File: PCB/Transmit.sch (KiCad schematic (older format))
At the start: 27 parts

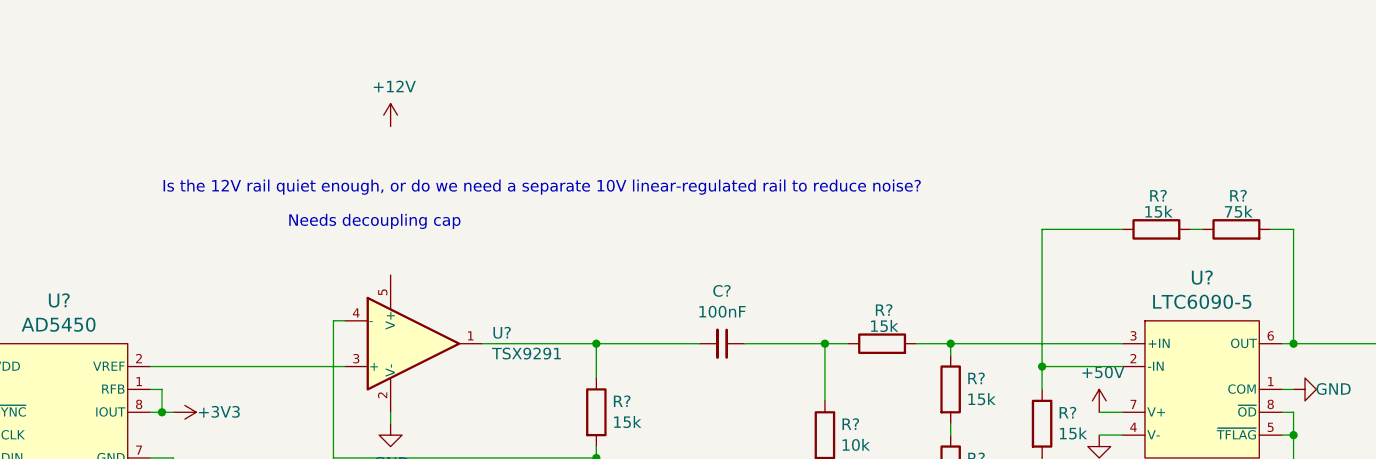
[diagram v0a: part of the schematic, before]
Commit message: Changed transmit-enable to connect to FPGA instead of microcontroller, added 10V linear regulator
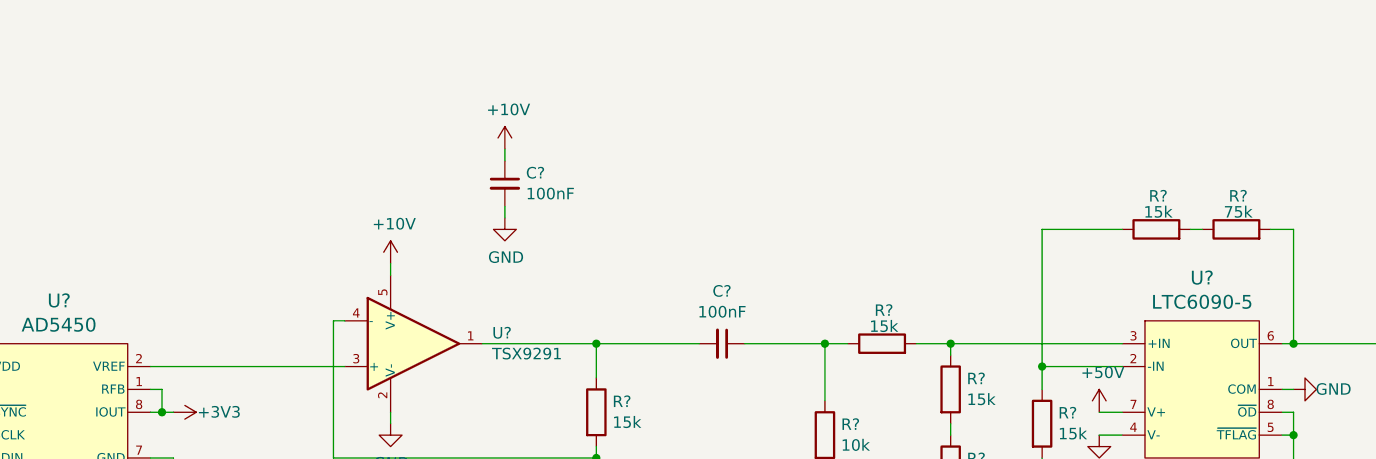
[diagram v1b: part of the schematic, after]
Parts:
- added C?: 100nF, Capacitors_SMD:C_0603_HandSoldering, symbol Device:C_Small
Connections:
- net GND: now also C?.2
- net +10V: now reaches U?.5 (V+)
- net +10V: now also C?.1
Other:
- note removed: "Is the 12V rail quiet enough, or do we need a separate 10V linear-regulated rail to reduce noise?"
- note removed: "Needs decoupling cap"
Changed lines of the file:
@@
 $EndComp
-$Comp
-L power:+12V #PWR?
-U 1 1 5DED5B08
-P 3700 2650
-F 0 "#PWR?" H 3700 2500 50  0001 C CNN
-F 1 "+12V" H 3715 2823 50  0000 C CNN
-F 2 "" H 3700 2650 50  0001 C CNN
-F 3 "" H 3700 2650 50  0001 C CNN
-	1    3700 2650
-	1    0    0    -1
-$EndComp
-Text Notes 2700 2950 0    50   ~ 0
-Is the 12V rail quiet enough, or do we need a separate 10V linear-regulated rail to reduce noise?
 $Comp
 L Device:R R?
@@
 Wire Wire Line
 	8650 5800 8650 5850
-Text Notes 3250 3100 0    50   ~ 0
-Needs decoupling cap
 $Comp
 L power:GND #PWR?
@@
 Wire Wire Line
 	800  3050 800  3100
+$Comp
+L power:+10V #PWR?
+U 1 1 5E0A0743
+P 3700 3250
+F 0 "#PWR?" H 3700 3100 50  0001 C CNN
+F 1 "+10V" H 3715 3423 50  0000 C CNN
+F 2 "" H 3700 3250 50  0001 C CNN
+F 3 "" H 3700 3250 50  0001 C CNN
+	1    3700 3250
+	1    0    0    -1
+$EndComp
+$Comp
+L Device:C_Small C?
+U 1 1 5E1245EE
+P 4200 2900
+F 0 "C?" H 4292 2946 50  0000 L CNN
+F 1 "100nF" H 4292 2855 50  0000 L CNN
+F 2 "Capacitors_SMD:C_0603_HandSoldering" H 4200 2900 50  0001 C CNN
+F 3 "https://www.digikey.ca/product-detail/en/samsung-electro-mechanics/CL10B104KB8NNNC/1276-1000-1-ND/3889086" H 4200 2900 50  0001 C CNN
+	1    4200 2900
+	1    0    0    -1
+$EndComp
+$Comp
+L power:+10V #PWR?
+U 1 1 5E124B96
+P 4200 2750
+F 0 "#PWR?" H 4200 2600 50  0001 C CNN
+F 1 "+10V" H 4215 2923 50  0000 C CNN
+F 2 "" H 4200 2750 50  0001 C CNN
+F 3 "" H 4200 2750 50  0001 C CNN
+	1    4200 2750
+	1    0    0    -1
+$EndComp
+Wire Wire Line
+	4200 2750 4200 2800
+$Comp
+L power:GND #PWR?
+U 1 1 5E1277BF
+P 4200 3050
+F 0 "#PWR?" H 4200 2800 50  0001 C CNN
+F 1 "GND" H 4205 2877 50  0000 C CNN
+F 2 "" H 4200 3050 50  0001 C CNN
+F 3 "" H 4200 3050 50  0001 C CNN
+	1    4200 3050
+	1    0    0    -1
+$EndComp
+Wire Wire Line
+	4200 3050 4200 3000
+Wire Wire Line
+	3700 3250 3700 3300
 $EndSCHEMATC

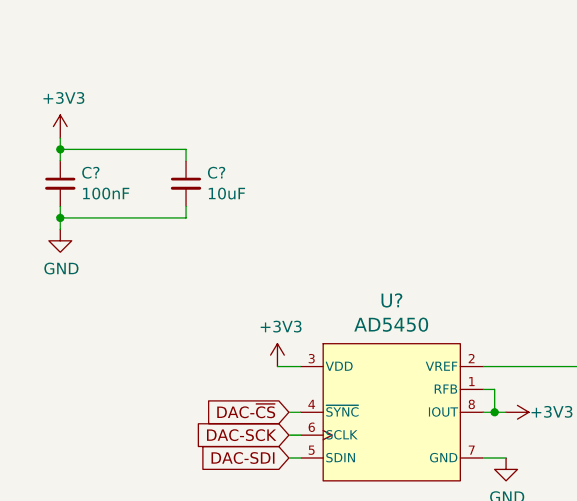
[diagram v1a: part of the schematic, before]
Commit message: Switch 3.3V analog circuitry to low noise supply, fix pin classifications on some parts, swap 9V connector for 10V
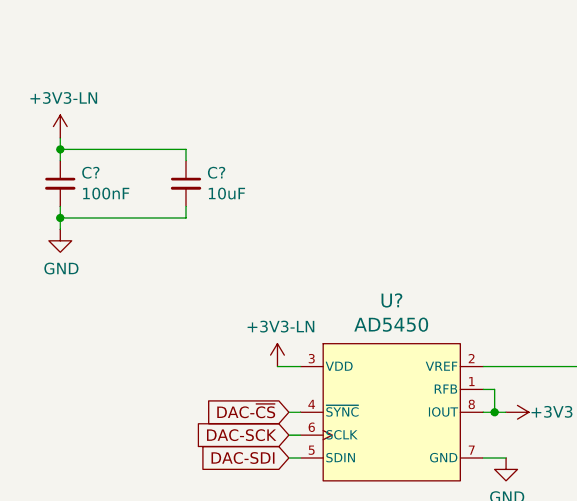
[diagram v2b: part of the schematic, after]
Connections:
- net +3V3: no longer C?.1, C?.1, U?.3 (VDD)
- new net +3V3-LN: C?.1, C?.1, U?.3 (VDD)
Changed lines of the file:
@@
-$EndComp
-$Comp
-L power:+3V3 #PWR?
-U 1 1 5DE63453
-P 1750 3700
-F 0 "#PWR?" H 1750 3550 50  0001 C CNN
-F 1 "+3V3" H 1765 3873 50  0000 C CNN
-F 2 "" H 1750 3700 50  0001 C CNN
-F 3 "" H 1750 3700 50  0001 C CNN
-	1    1750 3700
-	1    0    0    -1
 $EndComp
 $Comp
@@
 $EndComp
 $Comp
-L power:+3V3 #PWR?
-U 1 1 5E3B8767
-P 800 2700
-F 0 "#PWR?" H 800 2550 50  0001 C CNN
-F 1 "+3V3" H 815 2873 50  0000 C CNN
-F 2 "" H 800 2700 50  0001 C CNN
-F 3 "" H 800 2700 50  0001 C CNN
-	1    800  2700
-	1    0    0    -1
-$EndComp
-$Comp
 L Device:C_Small C?
 U 1 1 5E3BD08F
@@
 Wire Wire Line
 	3700 3250 3700 3300
+$Comp
+L Parts:+3V3-LN #PWR?
+U 1 1 5E29A668
+P 1750 3700
+F 0 "#PWR?" H 1750 3550 50  0001 C CNN
+F 1 "+3V3-LN" H 1765 3873 50  0000 C CNN
+F 2 "" H 1750 3700 50  0001 C CNN
+F 3 "" H 1750 3700 50  0001 C CNN
+	1    1750 3700
+	1    0    0    -1
+$EndComp
+$Comp
+L Parts:+3V3-LN #PWR?
+U 1 1 5E29D33A
+P 800 2700
+F 0 "#PWR?" H 800 2550 50  0001 C CNN
+F 1 "+3V3-LN" H 815 2873 50  0000 C CNN
+F 2 "" H 800 2700 50  0001 C CNN
+F 3 "" H 800 2700 50  0001 C CNN
+	1    800  2700
+	1    0    0    -1
+$EndComp
 $EndSCHEMATC

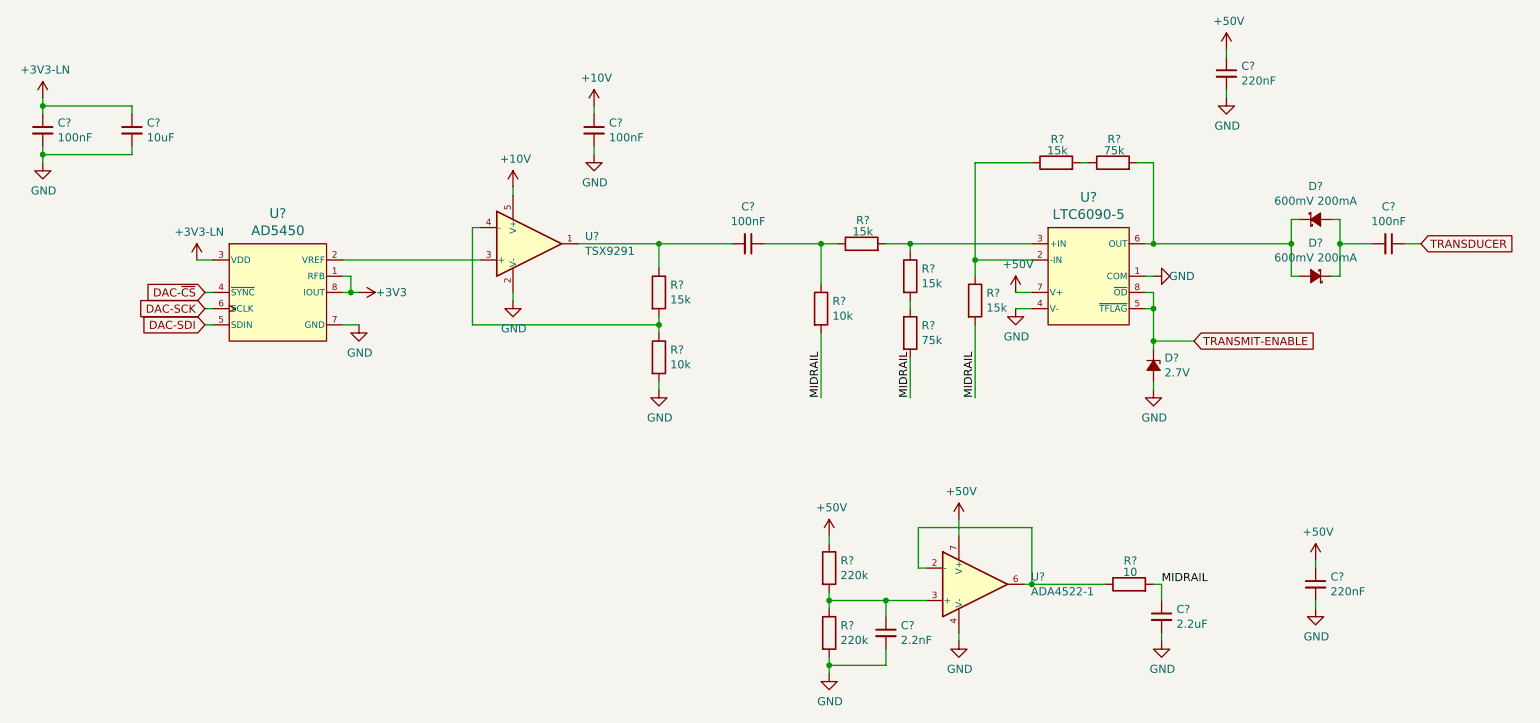
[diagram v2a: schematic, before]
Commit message: Annotate schematic, simplify transmit circuit, shuffle receive opamp stages, reorder buttons so they match net names, reorder connectors to simplify routing, begin arranging parts on PCB
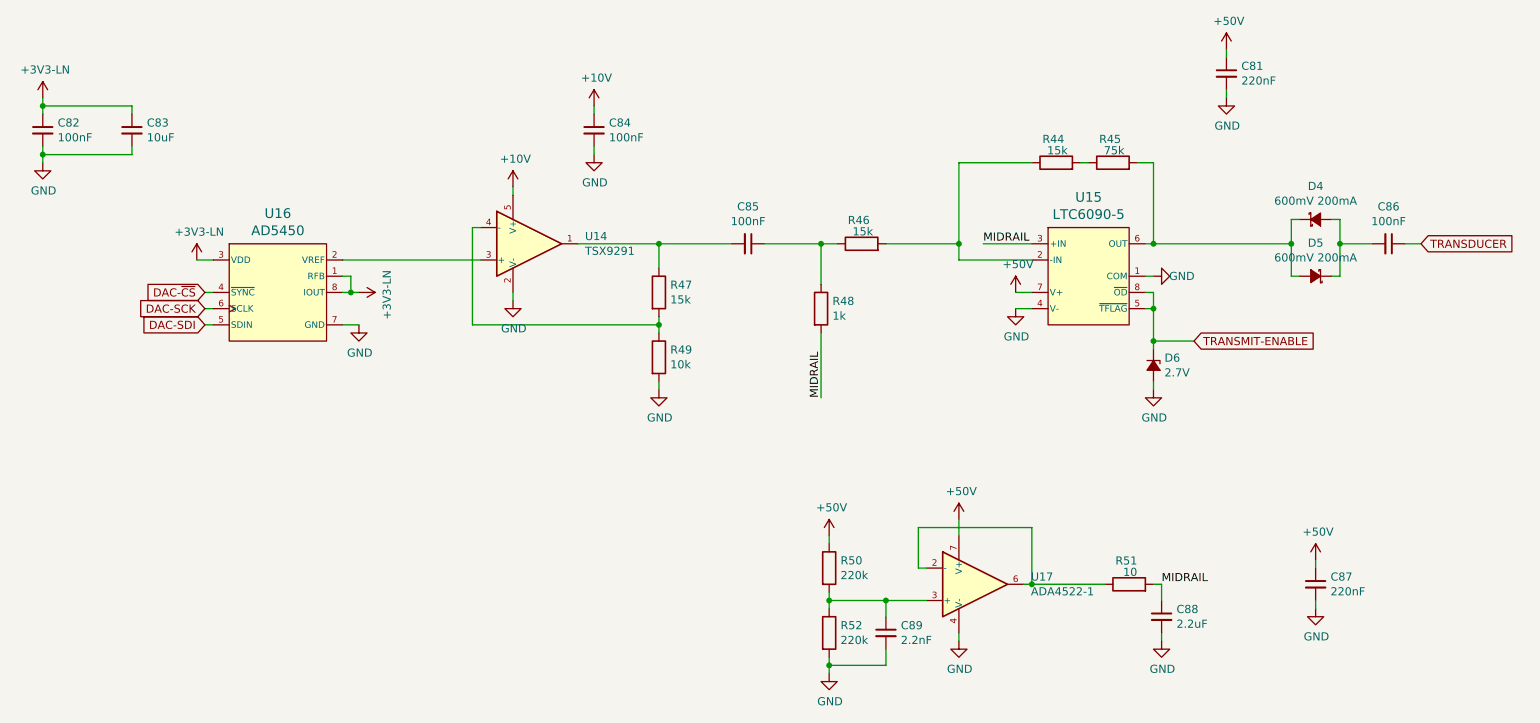
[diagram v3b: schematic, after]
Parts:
- removed R? (x2): 15k, Resistors_SMD:R_0603_HandSoldering, symbol Device:R
- removed R?: 75k, Resistors_SMD:R_0603_HandSoldering, symbol Device:R
- R48: renamed from R?; value 10k -> 1k
- gave numbers to parts that had none: 24
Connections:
- net +3V3 is gone; now on net +3V3-LN: U16.1 (RFB), U16.8 (IOUT)
- net MIDRAIL: now also U15.3 (+IN)
- net at R46.2: now also R44.1, U15.2 (-IN); no longer U15.3 (+IN)

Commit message: Begin layout around FPGA and microcontroller, rearrange some connections to FPGA and microcontroller, change groupings of optional debug pins
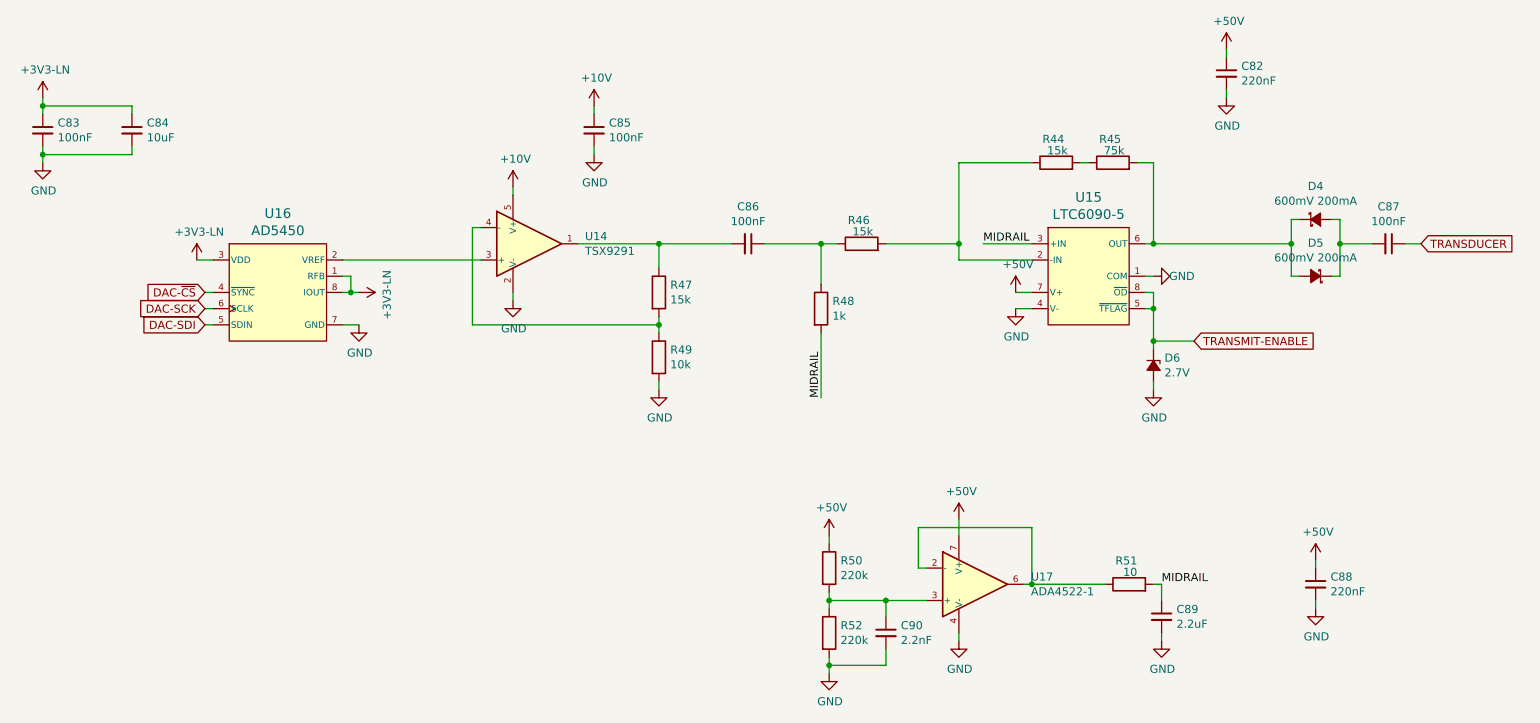
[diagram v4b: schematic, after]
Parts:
- renumbered C81 to C82, C82 to C83, C83 to C84, C84 to C85, C85 to C86, C86 to C87, C87 to C88, C88 to C89, C89 to C90
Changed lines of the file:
@@
 	2650 3700 3500 3700
 $Comp
-L Device:C_Small C85
+L Device:C_Small C86
 U 1 1 5DF03C94
 P 5150 3600
-F 0 "C85" V 4921 3600 50  0000 C CNN
+F 0 "C86" V 4921 3600 50  0000 C CNN
 F 1 "100nF" V 5012 3600 50  0000 C CNN
 F 2 "Capacitors_SMD:C_1206_HandSoldering" H 5150 3600 50  0001 C CNN
@@
 	6450 3100 6900 3100
 $Comp
-L Device:C_Small C86
+L Device:C_Small C87
 U 1 1 5DEF2296
 P 9100 3600
-F 0 "C86" V 8871 3600 50  0000 C CNN
+F 0 "C87" V 8871 3600 50  0000 C CNN
 F 1 "100nF" V 8962 3600 50  0000 C CNN
 F 2 "Capacitors_SMD:C_1206_HandSoldering" H 9100 3600 50  0001 C CNN
@@
 $EndComp
 $Comp
-L Device:C_Small C88
+L Device:C_Small C89
 U 1 1 5DF222FC
 P 7700 5900
-F 0 "C88" H 7792 5946 50  0000 L CNN
+F 0 "C89" H 7792 5946 50  0000 L CNN
 F 1 "2.2uF" H 7792 5855 50  0000 L CNN
 F 2 "Capacitors_SMD:C_1210_HandSoldering" H 7700 5900 50  0001 C CNN
@@
 	7700 5700 7700 5800
 $Comp
-L Device:C_Small C81
+L Device:C_Small C82
 U 1 1 5DF2730B
 P 8100 2550
-F 0 "C81" H 8192 2596 50  0000 L CNN
+F 0 "C82" H 8192 2596 50  0000 L CNN
 F 1 "220nF" H 8192 2505 50  0000 L CNN
 F 2 "Capacitors_SMD:C_1206_HandSoldering" H 8100 2550 50  0001 C CNN
@@
 	5650 5850 5650 5800
 $Comp
-L Device:C_Small C89
+L Device:C_Small C90
 U 1 1 5DF34700
 P 6000 6000
-F 0 "C89" H 6092 6046 50  0000 L CNN
+F 0 "C90" H 6092 6046 50  0000 L CNN
 F 1 "2.2nF" H 6092 5955 50  0000 L CNN
 F 2 "Capacitors_SMD:C_0603_HandSoldering" H 6000 6000 50  0001 C CNN
@@
 Connection ~ 7650 4000
 $Comp
-L Device:C_Small C87
+L Device:C_Small C88
 U 1 1 5DFB3BB1
 P 8650 5700
-F 0 "C87" H 8742 5746 50  0000 L CNN
+F 0 "C88" H 8742 5746 50  0000 L CNN
 F 1 "220nF" H 8742 5655 50  0000 L CNN
 F 2 "Capacitors_SMD:C_1206_HandSoldering" H 8650 5700 50  0001 C CNN
@@
 $EndComp
 $Comp
-L Device:C_Small C82
+L Device:C_Small C83
 U 1 1 5E3B80F6
 P 800 2900
-F 0 "C82" H 892 2946 50  0000 L CNN
+F 0 "C83" H 892 2946 50  0000 L CNN
 F 1 "100nF" H 892 2855 50  0000 L CNN
 F 2 "Capacitors_SMD:C_0603_HandSoldering" H 800 2900 50  0001 C CNN
@@
 $EndComp
 $Comp
-L Device:C_Small C83
+L Device:C_Small C84
 U 1 1 5E3BD08F
 P 1350 2900
-F 0 "C83" H 1442 2946 50  0000 L CNN
+F 0 "C84" H 1442 2946 50  0000 L CNN
 F 1 "10uF" H 1442 2855 50  0000 L CNN
 F 2 "Capacitors_SMD:C_0805_HandSoldering" H 1350 2900 50  0001 C CNN
@@
 $EndComp
 $Comp
-L Device:C_Small C84
+L Device:C_Small C85
 U 1 1 5E1245EE
 P 4200 2900
-F 0 "C84" H 4292 2946 50  0000 L CNN
+F 0 "C85" H 4292 2946 50  0000 L CNN
 F 1 "100nF" H 4292 2855 50  0000 L CNN
 F 2 "Capacitors_SMD:C_0603_HandSoldering" H 4200 2900 50  0001 C CNN
